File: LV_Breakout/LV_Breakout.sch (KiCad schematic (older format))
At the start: 24 parts, among them J1 B10B-PHDSS(LF)(SN), J2 DF22-2P-7.92DSA(05), J3 TE 1-770872-0, J4 TE 776228-1, K1 T9VV1K15-12S, U1 R-78E5.0-0.5

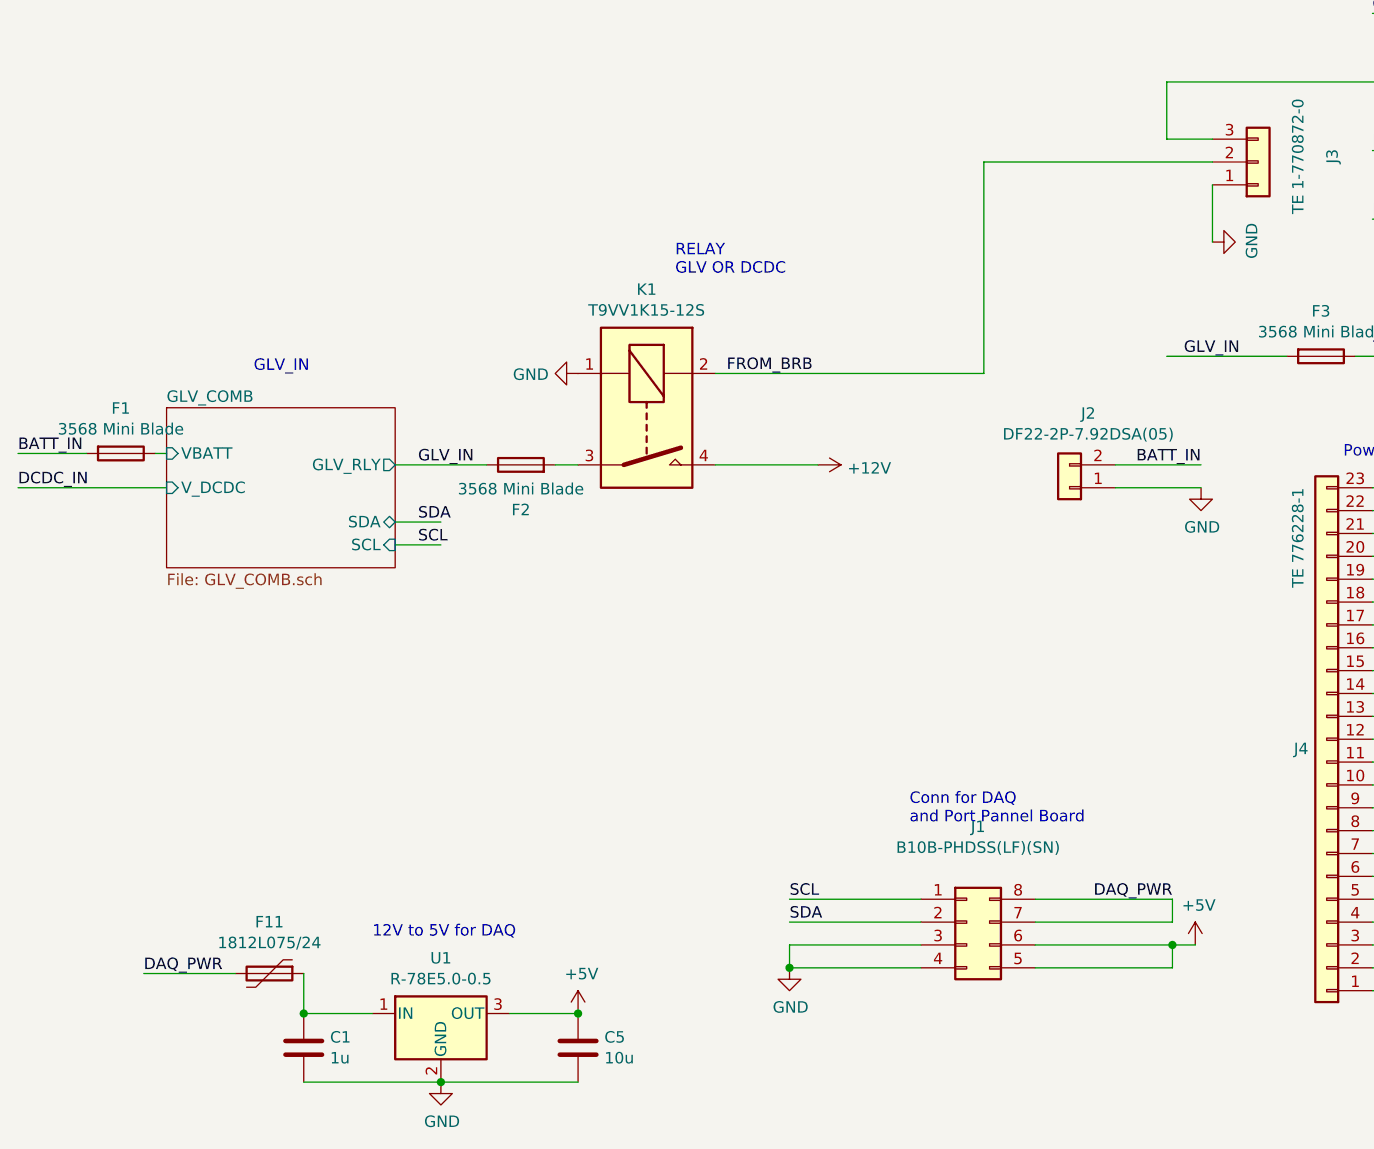
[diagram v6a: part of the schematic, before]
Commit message: change pcb trace
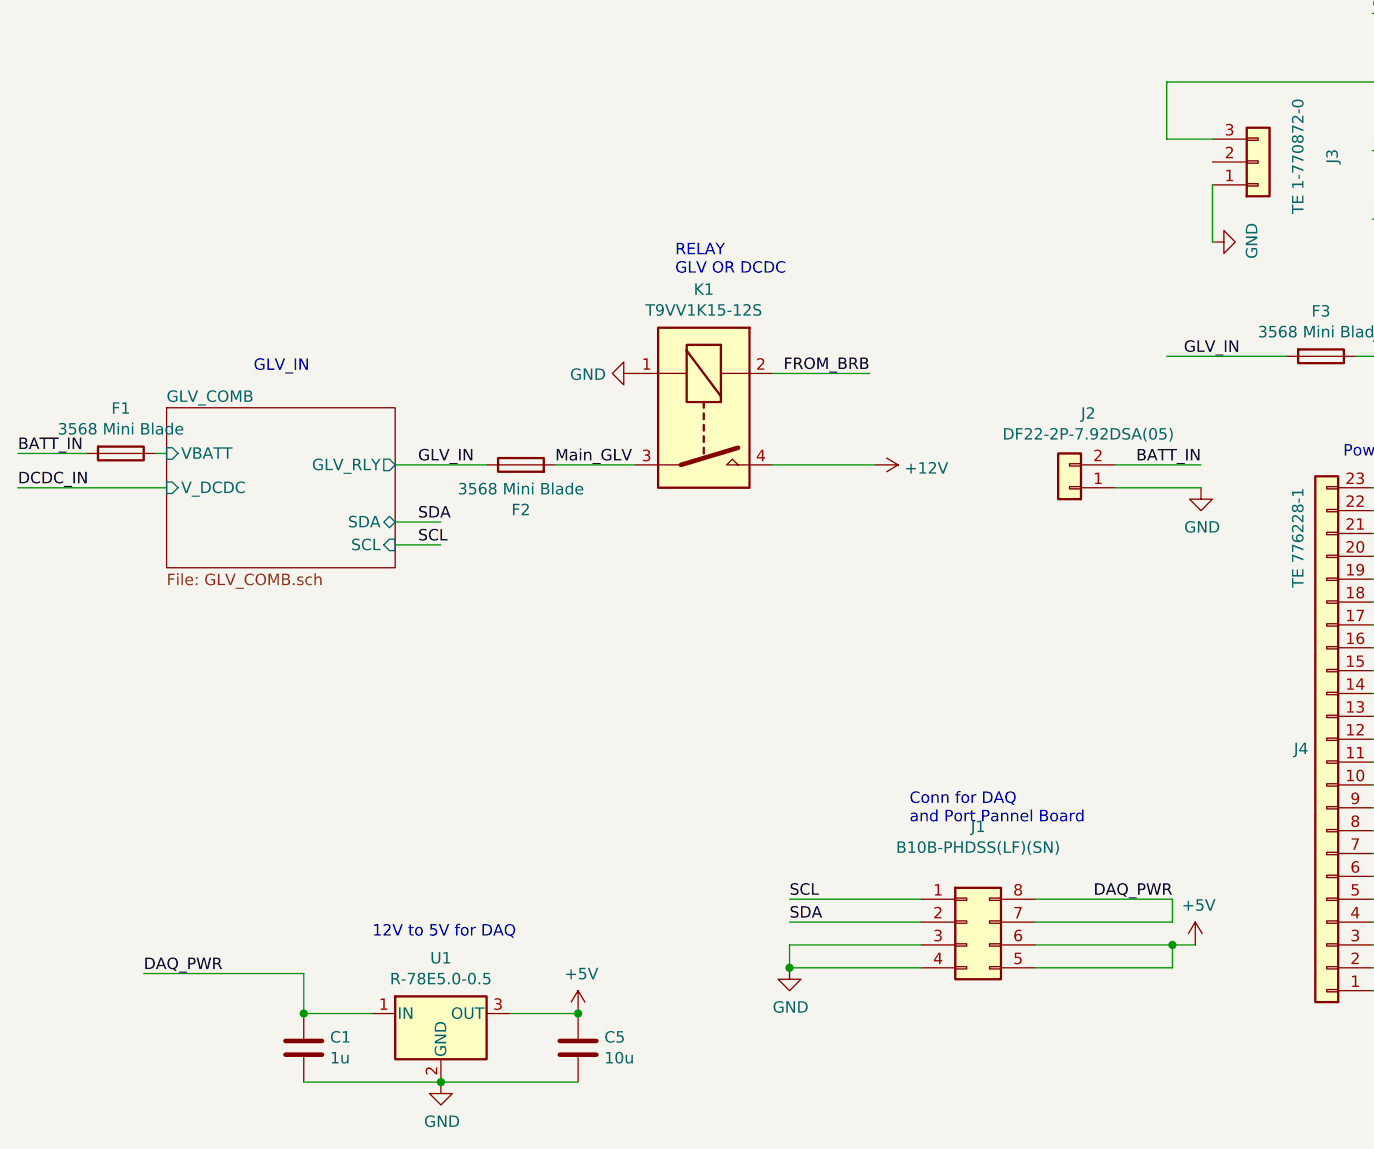
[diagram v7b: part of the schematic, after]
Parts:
- removed F11: 1812L075/24, Fuse:Fuse_1812_4532Metric_Pad1.30x3.40mm_HandSolder, symbol Device:Polyfuse
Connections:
- net labels added: Main_GLV
- wire segments 99 -> 97
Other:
- moved on the sheet: K1
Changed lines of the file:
@@
 L power:GND #PWR03
 U 1 1 5E5DA536
-P 5625 3500
-F 0 "#PWR03" H 5625 3250 50  0001 C CNN
-F 1 "GND" V 5630 3372 50  0000 R CNN
-F 2 "" H 5625 3500 50  0001 C CNN
-F 3 "" H 5625 3500 50  0001 C CNN
-	1    5625 3500
-	0    1    1    0
-$EndComp
-Text Label 6275 3500 0    50   ~ 0
+P 5875 3500
+F 0 "#PWR03" H 5875 3250 50  0001 C CNN
+F 1 "GND" V 5880 3372 50  0000 R CNN
+F 2 "" H 5875 3500 50  0001 C CNN
+F 3 "" H 5875 3500 50  0001 C CNN
+	1    5875 3500
+	0    1    1    0
+$EndComp
+Text Label 6900 3500 2    50   ~ 0
 FROM_BRB
 Wire Wire Line
-	5525 3900 5625 3900
+	5525 3900 5875 3900
 $Comp
 L power:+12V #PWR05
 U 1 1 5E5F9121
-P 6675 3900
-F 0 "#PWR05" H 6675 3750 50  0001 C CNN
-F 1 "+12V" V 6690 4028 50  0000 L CNN
-F 2 "" H 6675 3900 50  0001 C CNN
-F 3 "" H 6675 3900 50  0001 C CNN
-	1    6675 3900
+P 6925 3900
+F 0 "#PWR05" H 6925 3750 50  0001 C CNN
+F 1 "+12V" V 6940 4028 50  0000 L CNN
+F 2 "" H 6925 3900 50  0001 C CNN
+F 3 "" H 6925 3900 50  0001 C CNN
+	1    6925 3900
 	0    1    1    0
 $EndComp
@@
 VCAP_AB
 Wire Wire Line
-	6675 3900 6225 3900
+	6925 3900 6475 3900
 $Comp
 L Device:Fuse F5
@@
 L AERO_custom_symbols:T9VV1K15-12S K1
 U 1 1 5E5C42EC
-P 5925 3700
-F 0 "K1" V 5358 3700 50  0000 C CNN
-F 1 "T9VV1K15-12S" V 5449 3700 50  0000 C CNN
-F 2 "AERO_FOOT:RELAY_T9VV1K15-12S" H 6275 3650 50  0001 L CNN
-F 3 "https://www.te.com/commerce/DocumentDelivery/DDEController?Action=srchrtrv&DocNm=Power_PCB_Relay_T9V_Solar&DocType=DS&DocLang=English" H 5925 3700 50  0001 C CNN
-	1    5925 3700
+P 6175 3700
+F 0 "K1" V 5608 3700 50  0000 C CNN
+F 1 "T9VV1K15-12S" V 5699 3700 50  0000 C CNN
+F 2 "AERO_FOOT:RELAY_T9VV1K15-12S" H 6525 3650 50  0001 L CNN
+F 3 "https://www.te.com/commerce/DocumentDelivery/DDEController?Action=srchrtrv&DocNm=Power_PCB_Relay_T9V_Solar&DocType=DS&DocLang=English" H 6175 3700 50  0001 C CNN
+	1    6175 3700
 	0    1    1    0
 $EndComp
@@
 	8200 2225 9475 2225
 Wire Wire Line
-	6225 3500 7400 3500
-Wire Wire Line
-	7400 3500 7400 2575
-Wire Wire Line
-	7400 2575 8400 2575
-Wire Wire Line
 	8200 2475 8400 2475
-$Comp
-L Device:Polyfuse F11
-U 1 1 5E5ACD10
-P 4275 6125
-F 0 "F11" V 4050 6125 50  0000 C CNN
-F 1 "1812L075/24" V 4141 6125 50  0000 C CNN
-F 2 "Fuse:Fuse_1812_4532Metric_Pad1.30x3.40mm_HandSolder" H 4325 5925 50  0001 L CNN
-F 3 "~" H 4275 6125 50  0001 C CNN
-	1    4275 6125
-	0    1    1    0
-$EndComp
-Wire Wire Line
-	3725 6125 4125 6125
+Wire Wire Line
+	6475 3500 6900 3500
+Wire Wire Line
+	3725 6125 4425 6125
+Text Label 5525 3900 0    50   ~ 0
+Main_GLV
 $EndSCHEMATC

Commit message: Minor Layout Changes
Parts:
- J2: footprint Connector_JST:JST_VH_B2P3-VH_1x02_P7.92mm_Vertical -> AERO_FOOT:DF22-2P-7.92DSA05
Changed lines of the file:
@@
 F 0 "J2" H 7693 3675 50  0000 C CNN
 F 1 "DF22-2P-7.92DSA(05)" H 7693 3766 50  0000 C CNN
-F 2 "Connector_JST:JST_VH_B2P3-VH_1x02_P7.92mm_Vertical" H 7775 4000 50  0001 C CNN
+F 2 "AERO_FOOT:DF22-2P-7.92DSA05" H 7775 4000 50  0001 C CNN
 F 3 "~" H 7775 4000 50  0001 C CNN
 	1    7775 4000
